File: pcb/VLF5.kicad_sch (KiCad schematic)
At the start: 19 parts, among them CN1 532610571, U1 STM32H743VIHx, X1 X322516MLB4SI

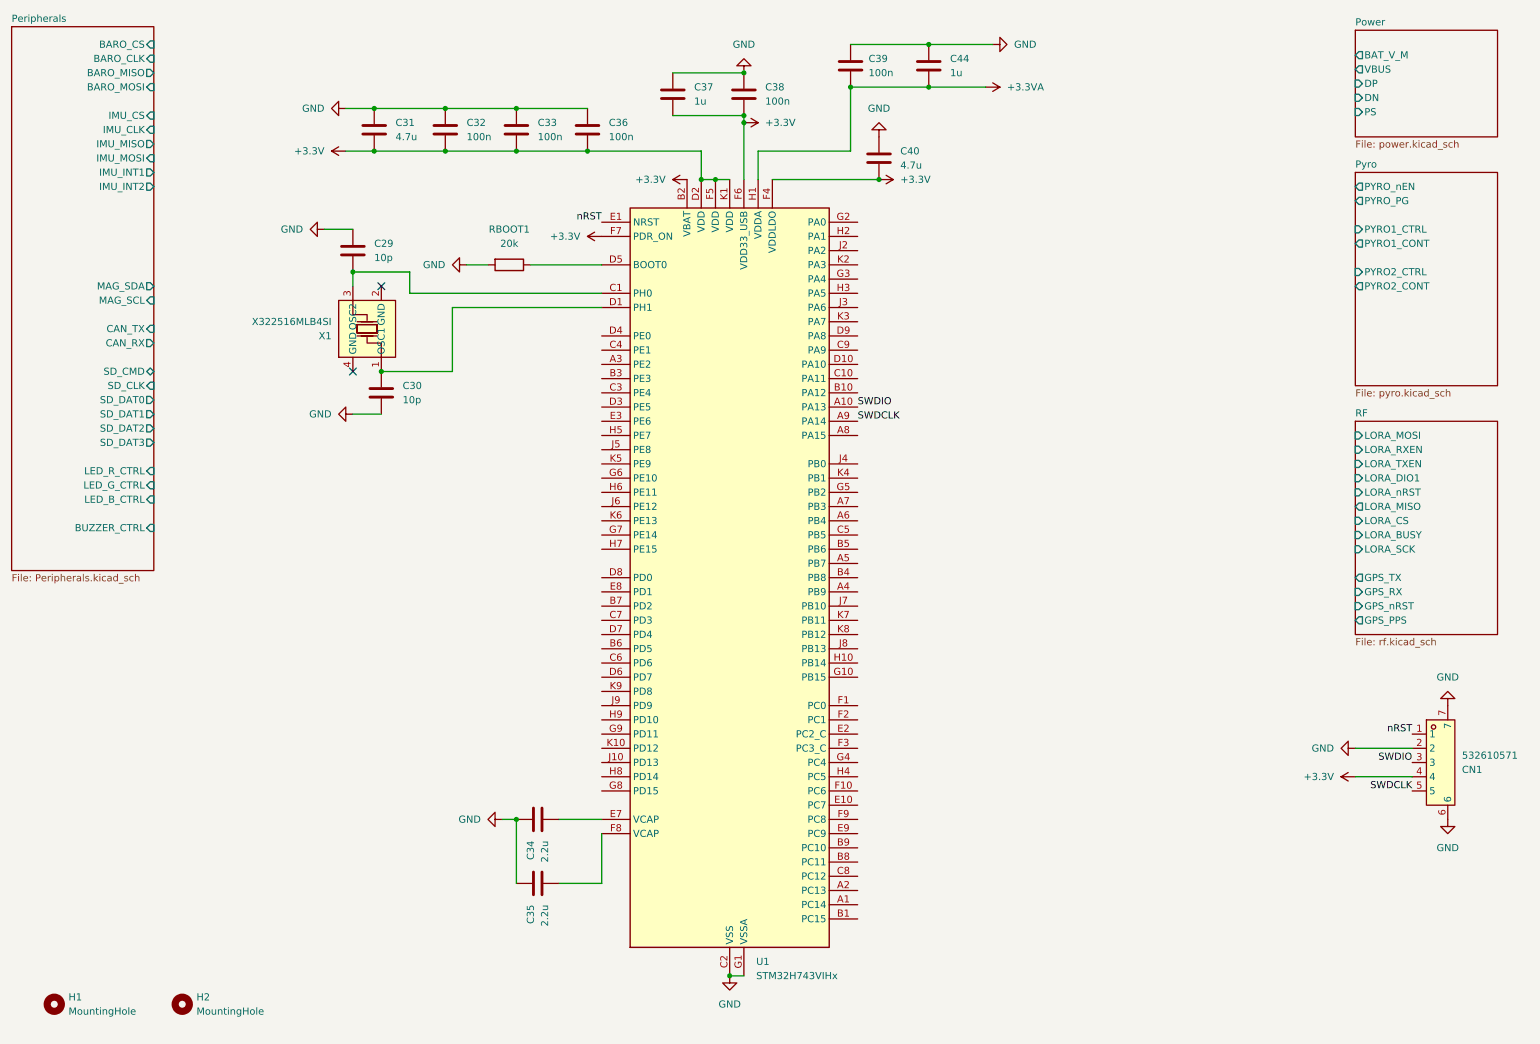
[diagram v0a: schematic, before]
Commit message: add pull up resistor for sd, change pad net
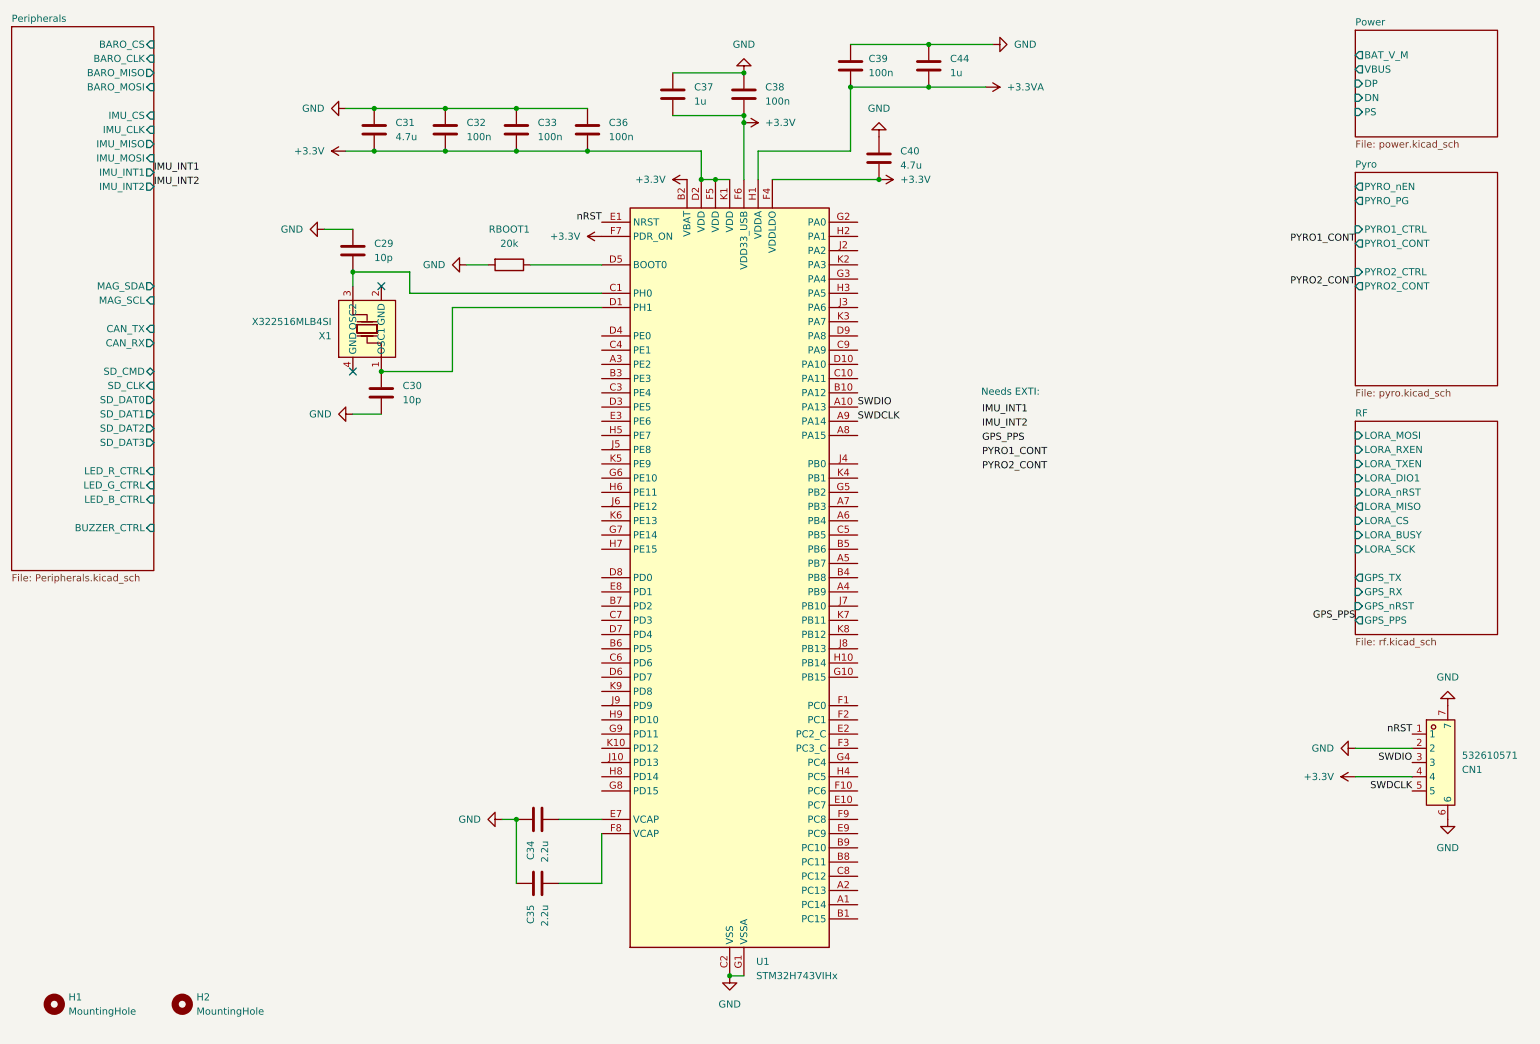
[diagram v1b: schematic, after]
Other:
- note added: "Needs EXTI:"
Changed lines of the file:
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@@
+		)
+	)
+	(text "Needs EXTI:"
+		(exclude_from_sim no)
+		(at 192.405 83.82 0)
+		(effects
+			(font
+				(size 1.27 1.27)
+			)
+		)
+	)
+	(label "PYRO1_CONT"
+		(at 187.325 95.25 0)
+		(effects
+			(font
+				(size 1.27 1.27)
+			)
+			(justify left bottom)
 		)
 	)
@@
 		)
 	)
+	(label "IMU_INT1"
+		(at 39.37 44.45 0)
+		(effects
+			(font
+				(size 1.27 1.27)
+			)
+			(justify left bottom)
+		)
+	)
+	(label "IMU_INT2"
+		(at 39.37 46.99 0)
+		(effects
+			(font
+				(size 1.27 1.27)
+			)
+			(justify left bottom)
+		)
+	)
 	(label "SWDIO"
 		(at 264.16 149.86 180)
@@
 			)
 			(justify right bottom)
+		)
+	)
+	(label "PYRO2_CONT"
+		(at 187.325 97.79 0)
+		(effects
+			(font
+				(size 1.27 1.27)
+			)
+			(justify left bottom)
+		)
+	)
+	(label "GPS_PPS"
+		(at 187.325 92.71 0)
+		(effects
+			(font
+				(size 1.27 1.27)
+			)
+			(justify left bottom)
+		)
+	)
+	(label "IMU_INT1"
+		(at 187.325 87.63 0)
+		(effects
+			(font
+				(size 1.27 1.27)
+			)
+			(justify left bottom)
 		)
 	)
@@
 		)
 	)
+	(label "GPS_PPS"
+		(at 254 124.46 180)
+		(effects
+			(font
+				(size 1.27 1.27)
+			)
+			(justify right bottom)
+		)
+	)
 	(label "SWDCLK"
 		(at 264.16 154.94 180)
+		(effects
+			(font
+				(size 1.27 1.27)
+			)
+			(justify right bottom)
+		)
+	)
+	(label "IMU_INT2"
+		(at 187.325 90.17 0)
+		(effects
+			(font
+				(size 1.27 1.27)
+			)
+			(justify left bottom)
+		)
+	)
+	(label "PYRO2_CONT"
+		(at 254 64.77 180)
 		(effects
 			(font
@@
 		(effects
 			(font
+				(size 1.27 1.27)
+			)
+			(justify right bottom)
+		)
+	)
+	(label "PYRO1_CONT"
+		(at 254 57.15 180)
+		(effects
+			(font

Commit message: Original Layout with Pins Configured
🙏
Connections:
- net GPS_PPS: now also U1.A8 (PA15)
- net IMU_INT1: now also U1.A1 (PC14)
- net IMU_INT2: now also U1.A4 (PB9)
- net PYRO1_CONT: now also U1.J10 (PD13)
- net PYRO2_CONT: now also U1.K10 (PD12)
- net IMU_CS: now reaches U1.A2 (PC13)
- net IMU_CLK: now reaches U1.A3 (PE2)
- net MAG_SDA: now reaches U1.A5 (PB7)
- net LORA_MISO: now reaches U1.A6 (PB4)
- net LORA_SCK: now reaches U1.A7 (PB3)
- net BUZZER_CTRL: now reaches U1.B1 (PC15)
- net DP: now reaches U1.B10 (PA12)
- net MAG_SCL: now reaches U1.B4 (PB8)
- net GPS_TX: now reaches U1.B5 (PB6)
- net LORA_nRST: now reaches U1.B6 (PD5)
- net SD_CMD: now reaches U1.B7 (PD2)
- net SD_DAT3: now reaches U1.B8 (PC11)
- net SD_DAT2: now reaches U1.B9 (PC10)
- net DN: now reaches U1.C10 (PA11)
- net BARO_MOSI: now reaches U1.C5 (PB5)
- net LORA_MOSI: now reaches U1.C6 (PD6)
- net LORA_BUSY: now reaches U1.C7 (PD3)
- net SD_CLK: now reaches U1.C8 (PC12)
- net VBUS: now reaches U1.C9 (PA9)
- net GPS_RX: now reaches U1.D10 (PA10)
- net IMU_MISO: now reaches U1.D3 (PE5)
- net LORA_CS: now reaches U1.D7 (PD4)
- net LORA_RXEN: now reaches U1.D8 (PD0)
- net LORA_DIO1: now reaches U1.D9 (PA8)
- net GPS_nRST: now reaches U1.E10 (PC7)
- net IMU_MOSI: now reaches U1.E3 (PE6)
- net LORA_TXEN: now reaches U1.E8 (PD1)
- net SD_DAT1: now reaches U1.E9 (PC9)
- net BARO_CS: now reaches U1.F10 (PC6)
- net SD_DAT0: now reaches U1.F9 (PC8)
- net PYRO_nEN: now reaches U1.G9 (PD11)
- net BARO_CLK: now reaches U1.H3 (PA5)
- net PYRO_PG: now reaches U1.H9 (PD10)
- net BARO_MISO: now reaches U1.J3 (PA6)
- net BAT_V_M: now reaches U1.J4 (PB0)
- net CAN_TX: now reaches U1.J8 (PB13)
- net PYRO2_CTRL: now reaches U1.J9 (PD9)
- net LED_R_CTRL: now reaches U1.K2 (PA3)
- net LED_G_CTRL: now reaches U1.K3 (PA7)
- net LED_B_CTRL: now reaches U1.K4 (PB1)
- net PS: now reaches U1.K6 (PE13)
- net CAN_RX: now reaches U1.K8 (PB12)
- net PYRO1_CTRL: now reaches U1.K9 (PD8)
- no-connect marks 2 -> 3
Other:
- note removed: "Needs EXTI:"

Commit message: Iterating
Iterating
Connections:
- net BARO_MOSI: now also U1.D6 (PD7); no longer U1.C5 (PB5)
- net CAN_RX: now also U1.C5 (PB5); no longer U1.K8 (PB12)
- net CAN_TX: now also U1.B5 (PB6); no longer U1.J8 (PB13)
- net GPS_TX: now also U1.H10 (PB14); no longer U1.B5 (PB6)
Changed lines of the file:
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@@
+		)
+	)
+	(label "BARO_MOSI"
+		(at 119.38 134.62 180)
+		(effects
+			(font
+				(size 1.27 1.27)
+			)
+			(justify right bottom)
 		)
 	)
@@
 		)
 	)
+	(label "CAN_RX"
+		(at 165.1 109.22 0)
+		(effects
+			(font
+				(size 1.27 1.27)
+			)
+			(justify left bottom)
+		)
+	)
 	(label "LORA_nRST"
 		(at 254 101.6 180)
@@
 		)
 	)
-	(label "CAN_RX"
-		(at 165.1 127 0)
-		(effects
-			(font
-				(size 1.27 1.27)
-			)
-			(justify left bottom)
-		)
-	)
 	(label "SWDCLK"
 		(at 264.16 154.94 180)
@@
 		)
 	)
+	(label "CAN_TX"
+		(at 165.1 111.76 0)
+		(effects
+			(font
+				(size 1.27 1.27)
+			)
+			(justify left bottom)
+		)
+	)
 	(label "SD_DAT2"
 		(at 165.1 165.1 0)
@@
 		)
 	)
-	(label "CAN_TX"
-		(at 165.1 129.54 0)
-		(effects
-			(font
-				(size 1.27 1.27)
-			)
-			(justify left bottom)
-		)
-	)
 	(label "GPS_PPS"
 		(at 165.1 91.44 0)
@@
 		)
 	)
+	(label "GPS_TX"
+		(at 165.1 132.08 0)
+		(effects
+			(font
+				(size 1.27 1.27)
+			)
+			(justify left bottom)
+		)
+	)
 	(label "LORA_MOSI"
 		(at 254 91.44 180)
@@
 		)
 	)
-	(label "BARO_MOSI"
-		(at 165.1 109.22 0)
-		(effects
-			(font
-				(size 1.27 1.27)
-			)
-			(justify left bottom)
-		)
-	)
 	(label "SD_DAT2"
 		(at 39.37 90.17 0)
@@
 		(effects
 			(font
-				(size 1.27 1.27)
-			)
-			(justify left bottom)
-		)
-	)
-	(label "GPS_TX"
-		(at 165.1 111.76 0)
-		(effects
-			(font

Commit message: Changed Pins new Layout
Changed Pins new Layout
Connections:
- net MAG_SCL: now also U1.J7 (PB10); no longer U1.B4 (PB8)
- net MAG_SDA: now also U1.K7 (PB11); no longer U1.A5 (PB7)
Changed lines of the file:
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@@
 	)
 	(label "MAG_SDA"
-		(at 165.1 114.3 0)
+		(at 165.1 124.46 0)
 		(effects
 			(font
@@
 		)
 	)
+	(label "MAG_SCL"
+		(at 165.1 121.92 0)
+		(effects
+			(font
+				(size 1.27 1.27)
+			)
+			(justify left bottom)
+		)
+	)
 	(label "SWDCLK"
 		(at 264.16 154.94 180)
@@
 		(effects
 			(font
-				(size 1.27 1.27)
-			)
-			(justify left bottom)
-		)
-	)
-	(label "MAG_SCL"
-		(at 165.1 116.84 0)
-		(effects
-			(font

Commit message: More Progress
- Decoupling Capacitors Layed out
- GPIO pins changed around for GPS and LoRa
- STM Pin Vias Placed
WARNING: ALTERED NO-NET PADS KEEP RESETTING TO NO-NET ENSURE NO ERRORS IN DRC.
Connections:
- net GPS_nRST: now also U1.C7 (PD3); no longer U1.E10 (PC7)
- net LED_B_CTRL: now also U1.K2 (PA3); no longer U1.K4 (PB1)
- net LED_R_CTRL: now also U1.K4 (PB1); no longer U1.K2 (PA3)
- net LORA_BUSY: now also U1.E8 (PD1); no longer U1.C7 (PD3)
- net LORA_CS: now also U1.E10 (PC7); no longer U1.D7 (PD4)
- net LORA_DIO1: now also U1.D7 (PD4); no longer U1.D9 (PA8)
- net LORA_RXEN: now also U1.D9 (PA8); no longer U1.D8 (PD0)
- net LORA_TXEN: now also U1.D8 (PD0); no longer U1.E8 (PD1)

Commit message: VLF5 Rough Finish
Hallelujah
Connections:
- net LED_B_CTRL: now also U1.J2 (PA2); no longer U1.K2 (PA3)
- net PS: now also U1.K2 (PA3); no longer U1.K6 (PE13)
- net PYRO2_CONT: now also U1.J6 (PE12); no longer U1.K10 (PD12)
- net PYRO_PG: now also U1.K6 (PE13); no longer U1.H9 (PD10)
- net PYRO_nEN: now also U1.K5 (PE9); no longer U1.G9 (PD11)
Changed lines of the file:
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@@
-	(wire
-		(pts
-			(xy 106.68 124.46) (xy 119.38 124.46)
-		)
-		(stroke
-			(width 0)
-			(type default)
-		)
-	)
 	(wire
 		(pts
@@
 	(wire
 		(pts
-			(xy 106.68 119.38) (xy 119.38 119.38)
-		)
-		(stroke
-			(width 0)
-			(type default)
-		)
-	)
-	(wire
-		(pts
 			(xy 74.93 62.23) (xy 74.93 64.77)
 		)
@@
 	(wire
 		(pts
-			(xy 106.68 116.84) (xy 119.38 116.84)
-		)
-		(stroke
-			(width 0)
-			(type default)
-		)
-	)
-	(wire
-		(pts
 			(xy 111.76 171.45) (xy 119.38 171.45)
 		)
@@
 	(wire
 		(pts
-			(xy 106.68 129.54) (xy 119.38 129.54)
-		)
-		(stroke
-			(width 0)
-			(type default)
-		)
-	)
-	(wire
-		(pts
 			(xy 101.6 160.02) (xy 104.14 160.02)
 		)
@@
 	(wire
 		(pts
-			(xy 106.68 127) (xy 119.38 127)
-		)
-		(stroke
-			(width 0)
-			(type default)
-		)
-	)
-	(wire
-		(pts
-			(xy 177.8 157.48) (xy 165.1 157.48)
-		)
-		(stroke
-			(width 0)
-			(type default)
-		)
-	)
-	(wire
-		(pts
 			(xy 147.32 40.64) (xy 163.83 40.64)
 		)
@@
 		(pts
 			(xy 119.38 68.58) (xy 92.71 68.58)
-		)
-		(stroke
-			(width 0)
-			(type default)
-		)
-	)
-	(wire
-		(pts
-			(xy 177.8 73.66) (xy 165.1 73.66)
 		)
 		(stroke
@@
 	)
 	(label "LORA_RXEN"
-		(at 177.8 73.66 0)
+		(at 165.1 73.66 0)
 		(effects
 			(font
@@
 		)
 	)
-	(label "LED_B_CTRL"
-		(at 165.1 60.96 0)
-		(effects
-			(font
-				(size 1.27 1.27)
-			)
-			(justify left bottom)
-		)
-	)
 	(label "LORA_TXEN"
 		(at 254 96.52 180)
@@
 		)
 	)
+	(label "PYRO_nEN"
+		(at 119.38 96.52 180)
+		(effects
+			(font
+				(size 1.27 1.27)
+			)
+			(justify right bottom)
+		)
+	)
 	(label "LORA_BUSY"
-		(at 106.68 119.38 180)
+		(at 119.38 119.38 180)
 		(effects
 			(font
@@
 		)
 	)
-	(label "PYRO2_CONT"
-		(at 119.38 147.32 180)
+	(label "PS"
+		(at 165.1 60.96 0)
+		(effects
+			(font
+				(size 1.27 1.27)
+			)
+			(justify left bottom)
+		)
+	)
+	(label "PYRO_PG"
+		(at 119.38 106.68 180)
 		(effects
 			(font
@@
 		)
 	)
-	(label "PYRO_PG"
-		(at 119.38 142.24 180)
+	(label "PYRO2_CONT"
+		(at 119.38 104.14 180)
 		(effects
 			(font
@@
 		)
 	)
-	(label "PS"
-		(at 119.38 106.68 180)
-		(effects
-			(font
-				(size 1.27 1.27)
-			)
-			(justify right bottom)
-		)
-	)
 	(label "CAN_TX"
 		(at 165.1 111.76 0)
@@
 	)
 	(label "LORA_TXEN"
-		(at 106.68 116.84 180)
+		(at 119.38 116.84 180)
 		(effects
 			(font
@@
 	)
 	(label "LORA_nRST"
-		(at 106.68 129.54 180)
+		(at 119.38 129.54 180)
 		(effects
 			(font
@@
 	)
 	(label "LORA_CS"
-		(at 177.8 157.48 0)
+		(at 165.1 157.48 0)
 		(effects
 			(font
@@
 	)
 	(label "GPS_nRST"
-		(at 106.68 124.46 180)
+		(at 119.38 124.46 180)
 		(effects
 			(font
@@
 	)
 	(label "LORA_DIO1"
-		(at 106.68 127 180)
+		(at 119.38 127 180)
 		(effects
 			(font
@@
 		)
 	)
-	(label "PYRO_nEN"
-		(at 119.38 144.78 180)
-		(effects
-			(font
-				(size 1.27 1.27)
-			)
-			(justify right bottom)
-		)
-	)
 	(label "IMU_MISO"
 		(at 39.37 39.37 0)
 		(effects
 			(font
+				(size 1.27 1.27)
+			)
+			(justify left bottom)
+		)
+	)
+	(label "LED_B_CTRL"
+		(at 165.1 58.42 0)
+		(effects
+			(font

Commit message: cleanup
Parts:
- added NT1: NetTie_2, NetTie:NetTie-2_SMD_Pad0.5mm, symbol Device:NetTie_2
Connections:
- net GND: now also NT1.2; no longer C29.1, C30.2
- net GPS_RX: now also U1.H10 (PB14); no longer U1.D10 (PA10)
- net GPS_TX: now also U1.D10 (PA10); no longer U1.H10 (PB14)
- new net GND2: C29.1, C30.2, NT1.1
